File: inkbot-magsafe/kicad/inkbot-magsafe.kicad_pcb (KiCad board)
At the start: 4 copper layers, 91 x 77 mm, 0 parts

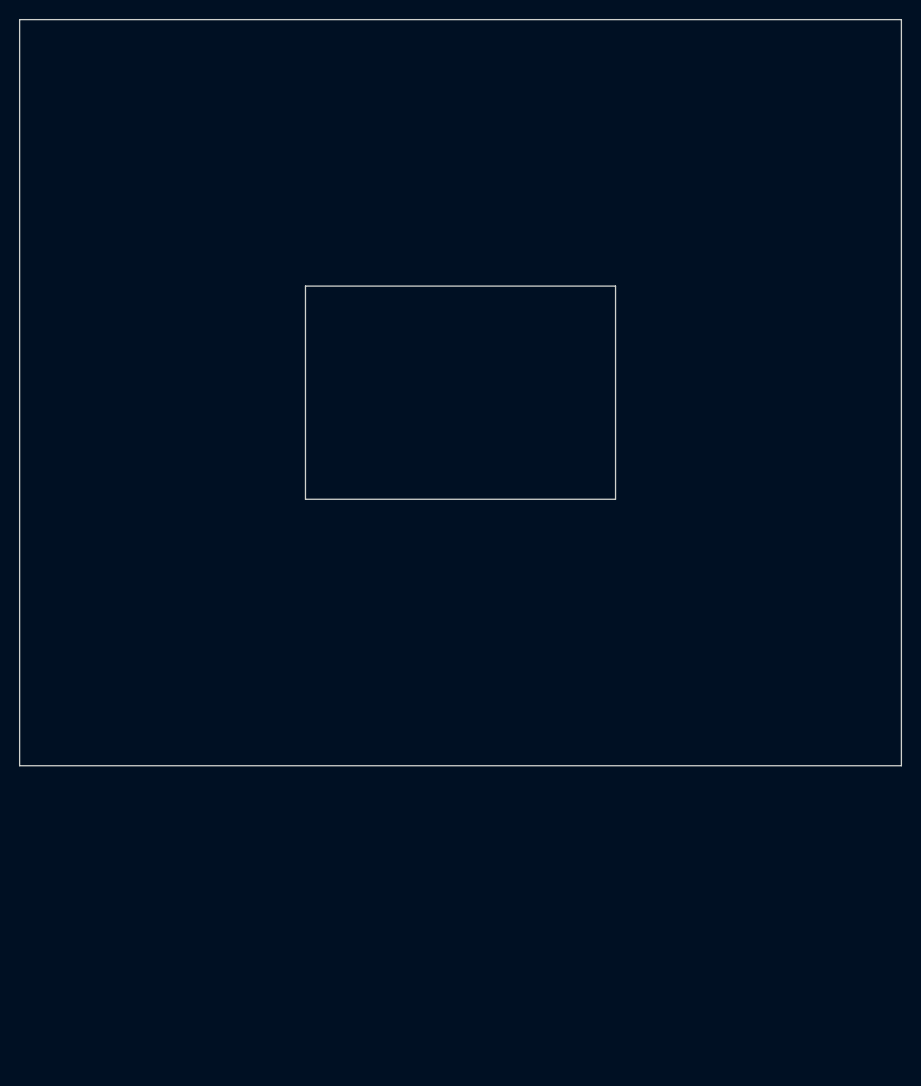
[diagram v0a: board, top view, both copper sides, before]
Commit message: inkbot-magsafe: portrait 3.7in panel, narrow board that fits the phone
Switch the panel to a 3.7-inch 240x416 portrait module (UC8253) so the tile is
57 mm wide and fits inside every MagSafe iPhone (minis included) with no side
overhang. Put the MagSafe ring high on the tile (center 30 mm from the top edge,
Apple's keep-in limit) so the body hangs below the rear-camera plateau; the
panel fills the tile and overlaps the ring (coil/magnets on the back). Update
firmware geometry (12,480-byte frame), BOM, docs, and the KiCad board outline.

Co-authored-by: Jason Hall <imjasonh@users.noreply.github.com>
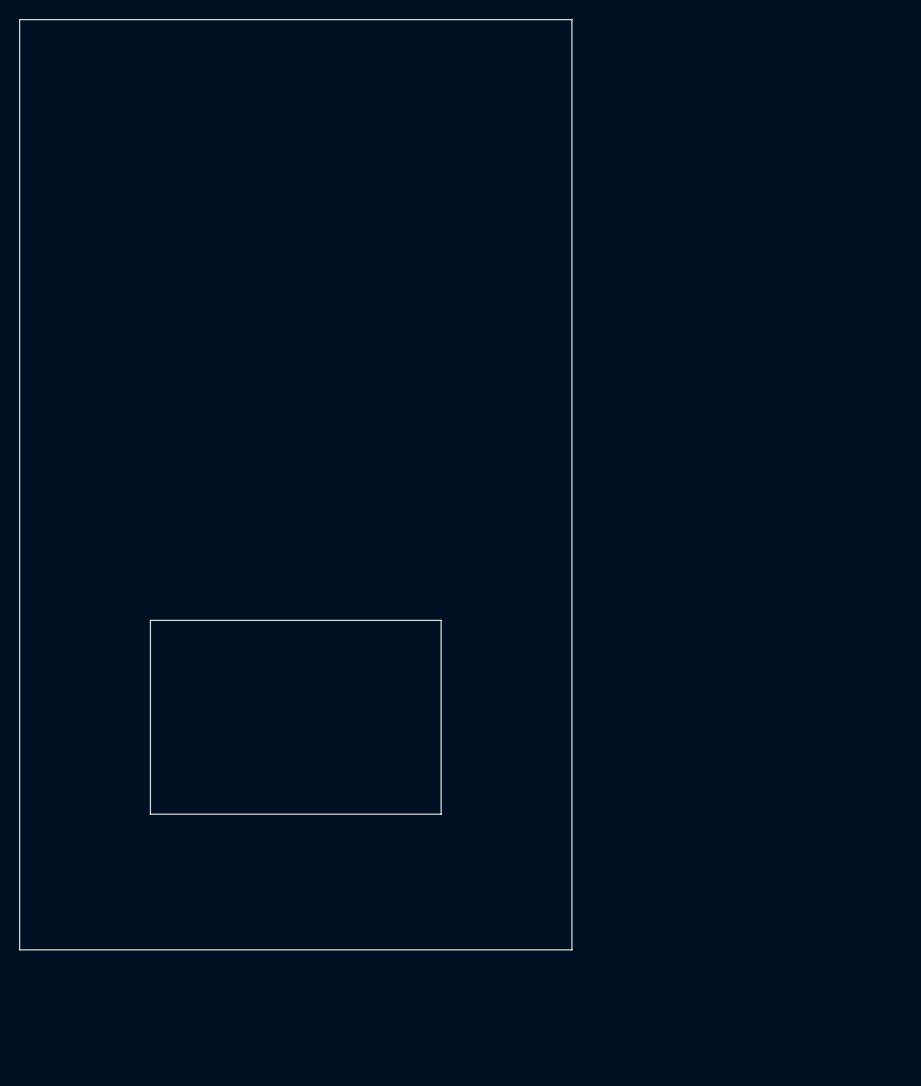
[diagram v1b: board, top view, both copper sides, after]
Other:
- board size 91 x 77 mm -> 57 x 96 mm
- board text added: "Qi coil"
- board text added: "panel 3.7in 240x416 (front, overlaps ring)"
- board text added: "top edge <=30mm above ring center: clears camera bump"
- board text removed: "Qi coil keep-in"
- board text removed: "inkbot-magsafe 0.4mm 4-layer no case"
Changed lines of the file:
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@@
     (title "inkbot-magsafe")
     (date "2026-09-06")
-    (rev "0.2.0")
-    (comment 1 "0.4 mm 4-layer; battery cutout; no case — panel is the front face")
-    (comment 2 "Place magnets + Qi coil on back; keep antenna outside magnet ring")
+    (rev "0.3.0")
+    (comment 1 "0.4 mm 4-layer; portrait; battery cutout; no case — panel is the front face")
+    (comment 2 "Ring high (30mm keep-in) clears cameras; panel overlaps ring; antenna at bottom edge")
   )
   (layers
@@
   )
   (net 0 "")
-  (gr_line (start 0.000 0.000) (end 91.000 0.000)
+  (gr_line (start 0.000 0.000) (end 57.000 0.000)
     (stroke (width 0.05) (type solid)) (layer "Edge.Cuts"))
-  (gr_line (start 91.000 0.000) (end 91.000 77.000)
+  (gr_line (start 57.000 0.000) (end 57.000 96.000)
     (stroke (width 0.05) (type solid)) (layer "Edge.Cuts"))
-  (gr_line (start 91.000 77.000) (end 0.000 77.000)
+  (gr_line (start 57.000 96.000) (end 0.000 96.000)
     (stroke (width 0.05) (type solid)) (layer "Edge.Cuts"))
-  (gr_line (start 0.000 77.000) (end 0.000 0.000)
+  (gr_line (start 0.000 96.000) (end 0.000 0.000)
     (stroke (width 0.05) (type solid)) (layer "Edge.Cuts"))
-  (gr_line (start 29.500 27.500) (end 61.500 27.500)
+  (gr_line (start 13.500 62.000) (end 43.500 62.000)
     (stroke (width 0.05) (type solid)) (layer "Edge.Cuts"))
-  (gr_line (start 61.500 27.500) (end 61.500 49.500)
+  (gr_line (start 43.500 62.000) (end 43.500 82.000)
     (stroke (width 0.05) (type solid)) (layer "Edge.Cuts"))
-  (gr_line (start 61.500 49.500) (end 29.500 49.500)
+  (gr_line (start 43.500 82.000) (end 13.500 82.000)
     (stroke (width 0.05) (type solid)) (layer "Edge.Cuts"))
-  (gr_line (start 29.500 49.500) (end 29.500 27.500)
+  (gr_line (start 13.500 82.000) (end 13.500 62.000)
     (stroke (width 0.05) (type solid)) (layer "Edge.Cuts"))
-  (gr_circle (center 45.500 38.500) (end 72.950 38.500)
+  (gr_line (start 2.000 1.500) (end 55.000 1.500)
+    (stroke (width 0.1) (type solid)) (layer "Cmts.User"))
+  (gr_line (start 55.000 1.500) (end 55.000 94.500)
+    (stroke (width 0.1) (type solid)) (layer "Cmts.User"))
+  (gr_line (start 55.000 94.500) (end 2.000 94.500)
+    (stroke (width 0.1) (type solid)) (layer "Cmts.User"))
+  (gr_line (start 2.000 94.500) (end 2.000 1.500)
+    (stroke (width 0.1) (type solid)) (layer "Cmts.User"))
+  (gr_circle (center 28.500 30.000) (end 55.950 30.000)
     (stroke (width 0.15) (type solid)) (fill none) (layer "Dwgs.User"))
-  (gr_circle (center 45.500 38.500) (end 65.500 38.500)
+  (gr_circle (center 28.500 30.000) (end 48.500 30.000)
     (stroke (width 0.1) (type solid)) (fill none) (layer "Dwgs.User"))
-  (gr_text "MagSafe ring PCD" (at 45.500 9.550 0)
+  (gr_text "MagSafe ring PCD" (at 28.500 30.000 0)
     (layer "Dwgs.User")
     (effects (font (size 0.8 0.8) (thickness 0.15))))
-  (gr_text "Qi coil keep-in" (at 45.500 60.000 0)
+  (gr_text "Qi coil" (at 28.500 51.500 0)
+    (layer "Dwgs.User")
+    (effects (font (size 0.7 0.7) (thickness 0.15))))
+  (gr_text "LiPo cutout" (at 28.500 60.500 0)
     (layer "Dwgs.User")
     (effects (font (size 0.8 0.8) (thickness 0.15))))
-  (gr_text "LiPo cutout" (at 45.500 26.000 0)
-    (layer "Dwgs.User")
+  (gr_text "panel 3.7in 240x416 (front, overlaps ring)" (at 28.500 94.000 0)
+    (layer "Cmts.User")
+    (effects (font (size 0.7 0.7) (thickness 0.15))))
+  (gr_text "top edge <=30mm above ring center: clears camera bump" (at 2.000 2.000 0)
+    (layer "Cmts.User")
     (effects (font (size 0.8 0.8) (thickness 0.15))))
-  (gr_text "inkbot-magsafe 0.4mm 4-layer  no case" (at 2.000 2.000 0)
-    (layer "Cmts.User")
-    (effects (font (size 1.0 1.0) (thickness 0.15))))
 )

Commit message: inkbot-magsafe: 4.26in 480x800 panel + nRF52833; drop mini support
Maximize display for standard/Pro iPhones (minis dropped). Switch the panel to
the 4.26in GDEY0426T82 (480x800, SSD1677) — the largest mono e-paper that fits a
70.6mm iPhone in portrait — and the MCU to the nRF52833 (128KB RAM) to hold the
48KB framebuffer. Rework the schematic (QFN-40 pinout, verified netlist), the
board outline (66x108mm), firmware panel geometry, BOM, and docs. Add a phone
compatibility table to the design doc.

Co-authored-by: Jason Hall <imjasonh@users.noreply.github.com>
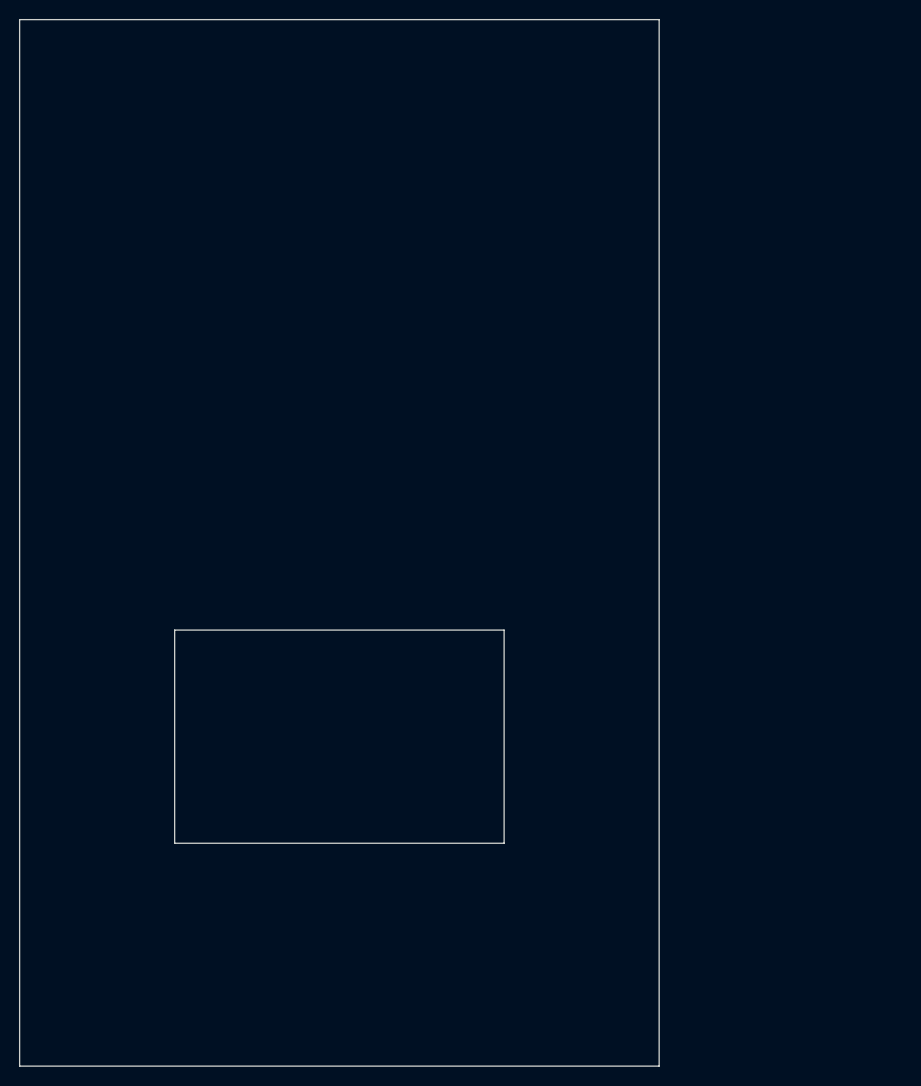
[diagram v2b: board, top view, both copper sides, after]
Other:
- board size 57 x 96 mm -> 66 x 108 mm
- board text added: "panel 4.26in 480x800 (front, overlaps ring)"
- board text removed: "panel 3.7in 240x416 (front, overlaps ring)"
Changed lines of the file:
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@@
   )
   (net 0 "")
-  (gr_line (start 0.000 0.000) (end 57.000 0.000)
+  (gr_line (start 0.000 0.000) (end 66.000 0.000)
     (stroke (width 0.05) (type solid)) (layer "Edge.Cuts"))
-  (gr_line (start 57.000 0.000) (end 57.000 96.000)
+  (gr_line (start 66.000 0.000) (end 66.000 108.000)
     (stroke (width 0.05) (type solid)) (layer "Edge.Cuts"))
-  (gr_line (start 57.000 96.000) (end 0.000 96.000)
+  (gr_line (start 66.000 108.000) (end 0.000 108.000)
     (stroke (width 0.05) (type solid)) (layer "Edge.Cuts"))
-  (gr_line (start 0.000 96.000) (end 0.000 0.000)
+  (gr_line (start 0.000 108.000) (end 0.000 0.000)
     (stroke (width 0.05) (type solid)) (layer "Edge.Cuts"))
-  (gr_line (start 13.500 62.000) (end 43.500 62.000)
+  (gr_line (start 16.000 63.000) (end 50.000 63.000)
     (stroke (width 0.05) (type solid)) (layer "Edge.Cuts"))
-  (gr_line (start 43.500 62.000) (end 43.500 82.000)
+  (gr_line (start 50.000 63.000) (end 50.000 85.000)
     (stroke (width 0.05) (type solid)) (layer "Edge.Cuts"))
-  (gr_line (start 43.500 82.000) (end 13.500 82.000)
+  (gr_line (start 50.000 85.000) (end 16.000 85.000)
     (stroke (width 0.05) (type solid)) (layer "Edge.Cuts"))
-  (gr_line (start 13.500 82.000) (end 13.500 62.000)
+  (gr_line (start 16.000 85.000) (end 16.000 63.000)
     (stroke (width 0.05) (type solid)) (layer "Edge.Cuts"))
-  (gr_line (start 2.000 1.500) (end 55.000 1.500)
+  (gr_line (start 1.815 1.500) (end 64.185 1.500)
     (stroke (width 0.1) (type solid)) (layer "Cmts.User"))
-  (gr_line (start 55.000 1.500) (end 55.000 94.500)
+  (gr_line (start 64.185 1.500) (end 64.185 106.830)
     (stroke (width 0.1) (type solid)) (layer "Cmts.User"))
-  (gr_line (start 55.000 94.500) (end 2.000 94.500)
+  (gr_line (start 64.185 106.830) (end 1.815 106.830)
     (stroke (width 0.1) (type solid)) (layer "Cmts.User"))
-  (gr_line (start 2.000 94.500) (end 2.000 1.500)
+  (gr_line (start 1.815 106.830) (end 1.815 1.500)
     (stroke (width 0.1) (type solid)) (layer "Cmts.User"))
-  (gr_circle (center 28.500 30.000) (end 55.950 30.000)
+  (gr_circle (center 33.000 30.000) (end 60.450 30.000)
     (stroke (width 0.15) (type solid)) (fill none) (layer "Dwgs.User"))
-  (gr_circle (center 28.500 30.000) (end 48.500 30.000)
+  (gr_circle (center 33.000 30.000) (end 53.000 30.000)
     (stroke (width 0.1) (type solid)) (fill none) (layer "Dwgs.User"))
-  (gr_text "MagSafe ring PCD" (at 28.500 30.000 0)
+  (gr_text "MagSafe ring PCD" (at 33.000 30.000 0)
     (layer "Dwgs.User")
     (effects (font (size 0.8 0.8) (thickness 0.15))))
-  (gr_text "Qi coil" (at 28.500 51.500 0)
+  (gr_text "Qi coil" (at 33.000 51.500 0)
     (layer "Dwgs.User")
     (effects (font (size 0.7 0.7) (thickness 0.15))))
-  (gr_text "LiPo cutout" (at 28.500 60.500 0)
+  (gr_text "LiPo cutout" (at 33.000 61.500 0)
     (layer "Dwgs.User")
     (effects (font (size 0.8 0.8) (thickness 0.15))))
-  (gr_text "panel 3.7in 240x416 (front, overlaps ring)" (at 28.500 94.000 0)
+  (gr_text "panel 4.26in 480x800 (front, overlaps ring)" (at 33.000 106.000 0)
     (layer "Cmts.User")
     (effects (font (size 0.7 0.7) (thickness 0.15))))

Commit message: inkbot-magsafe: drop 4.26in for 3.97in so it clears the phone bottom
The 4.26in module (105 mm tall) overhangs a 15 Pro by ~4 mm once the
MagSafe ring sits high enough to clear the cameras. Switch to the
GDEY0397T81P (56 x 97 mm, still 480x800 / SSD1677 / nRF52833) on a
60 x 99 mm board — ~5 mm bottom clearance on a 15 Pro.

Co-authored-by: Jason Hall <imjasonh@users.noreply.github.com>
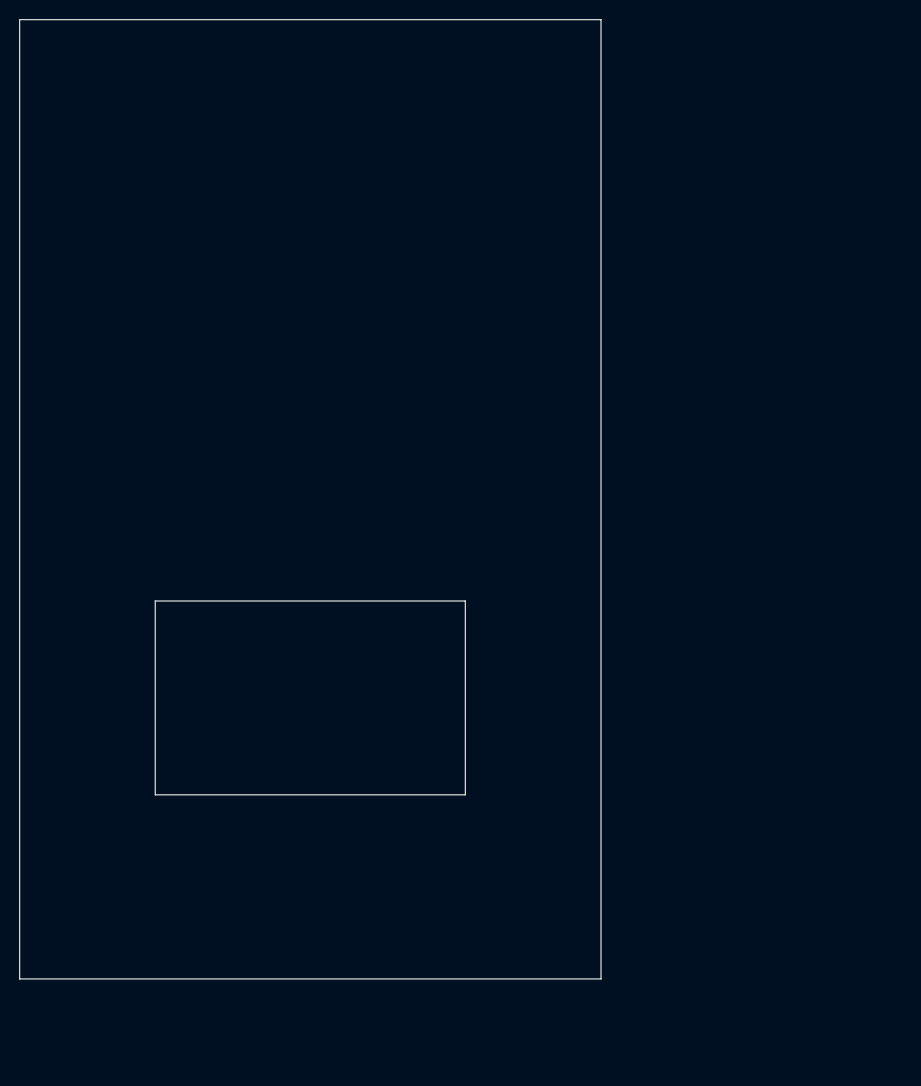
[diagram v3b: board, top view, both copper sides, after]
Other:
- board size 66 x 108 mm -> 60 x 99 mm
- board text added: "panel 3.97in 480x800 (front, overlaps ring)"
- board text removed: "panel 4.26in 480x800 (front, overlaps ring)"
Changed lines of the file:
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@@
   )
   (net 0 "")
-  (gr_line (start 0.000 0.000) (end 66.000 0.000)
+  (gr_line (start 0.000 0.000) (end 60.000 0.000)
     (stroke (width 0.05) (type solid)) (layer "Edge.Cuts"))
-  (gr_line (start 66.000 0.000) (end 66.000 108.000)
+  (gr_line (start 60.000 0.000) (end 60.000 99.000)
     (stroke (width 0.05) (type solid)) (layer "Edge.Cuts"))
-  (gr_line (start 66.000 108.000) (end 0.000 108.000)
+  (gr_line (start 60.000 99.000) (end 0.000 99.000)
     (stroke (width 0.05) (type solid)) (layer "Edge.Cuts"))
-  (gr_line (start 0.000 108.000) (end 0.000 0.000)
+  (gr_line (start 0.000 99.000) (end 0.000 0.000)
     (stroke (width 0.05) (type solid)) (layer "Edge.Cuts"))
-  (gr_line (start 16.000 63.000) (end 50.000 63.000)
+  (gr_line (start 14.000 60.000) (end 46.000 60.000)
     (stroke (width 0.05) (type solid)) (layer "Edge.Cuts"))
-  (gr_line (start 50.000 63.000) (end 50.000 85.000)
+  (gr_line (start 46.000 60.000) (end 46.000 80.000)
     (stroke (width 0.05) (type solid)) (layer "Edge.Cuts"))
-  (gr_line (start 50.000 85.000) (end 16.000 85.000)
+  (gr_line (start 46.000 80.000) (end 14.000 80.000)
     (stroke (width 0.05) (type solid)) (layer "Edge.Cuts"))
-  (gr_line (start 16.000 85.000) (end 16.000 63.000)
+  (gr_line (start 14.000 80.000) (end 14.000 60.000)
     (stroke (width 0.05) (type solid)) (layer "Edge.Cuts"))
-  (gr_line (start 1.815 1.500) (end 64.185 1.500)
+  (gr_line (start 1.880 1.200) (end 58.120 1.200)
     (stroke (width 0.1) (type solid)) (layer "Cmts.User"))
-  (gr_line (start 64.185 1.500) (end 64.185 106.830)
+  (gr_line (start 58.120 1.200) (end 58.120 97.820)
     (stroke (width 0.1) (type solid)) (layer "Cmts.User"))
-  (gr_line (start 64.185 106.830) (end 1.815 106.830)
+  (gr_line (start 58.120 97.820) (end 1.880 97.820)
     (stroke (width 0.1) (type solid)) (layer "Cmts.User"))
-  (gr_line (start 1.815 106.830) (end 1.815 1.500)
+  (gr_line (start 1.880 97.820) (end 1.880 1.200)
     (stroke (width 0.1) (type solid)) (layer "Cmts.User"))
-  (gr_circle (center 33.000 30.000) (end 60.450 30.000)
+  (gr_circle (center 30.000 30.000) (end 57.450 30.000)
     (stroke (width 0.15) (type solid)) (fill none) (layer "Dwgs.User"))
-  (gr_circle (center 33.000 30.000) (end 53.000 30.000)
+  (gr_circle (center 30.000 30.000) (end 50.000 30.000)
     (stroke (width 0.1) (type solid)) (fill none) (layer "Dwgs.User"))
-  (gr_text "MagSafe ring PCD" (at 33.000 30.000 0)
+  (gr_text "MagSafe ring PCD" (at 30.000 30.000 0)
     (layer "Dwgs.User")
     (effects (font (size 0.8 0.8) (thickness 0.15))))
-  (gr_text "Qi coil" (at 33.000 51.500 0)
+  (gr_text "Qi coil" (at 30.000 51.500 0)
     (layer "Dwgs.User")
     (effects (font (size 0.7 0.7) (thickness 0.15))))
-  (gr_text "LiPo cutout" (at 33.000 61.500 0)
+  (gr_text "LiPo cutout" (at 30.000 58.500 0)
     (layer "Dwgs.User")
     (effects (font (size 0.8 0.8) (thickness 0.15))))
-  (gr_text "panel 4.26in 480x800 (front, overlaps ring)" (at 33.000 106.000 0)
+  (gr_text "panel 3.97in 480x800 (front, overlaps ring)" (at 30.000 97.000 0)
     (layer "Cmts.User")
     (effects (font (size 0.7 0.7) (thickness 0.15))))
